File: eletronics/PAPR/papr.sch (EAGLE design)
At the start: 4 parts, among them Q1 FQP30N06L

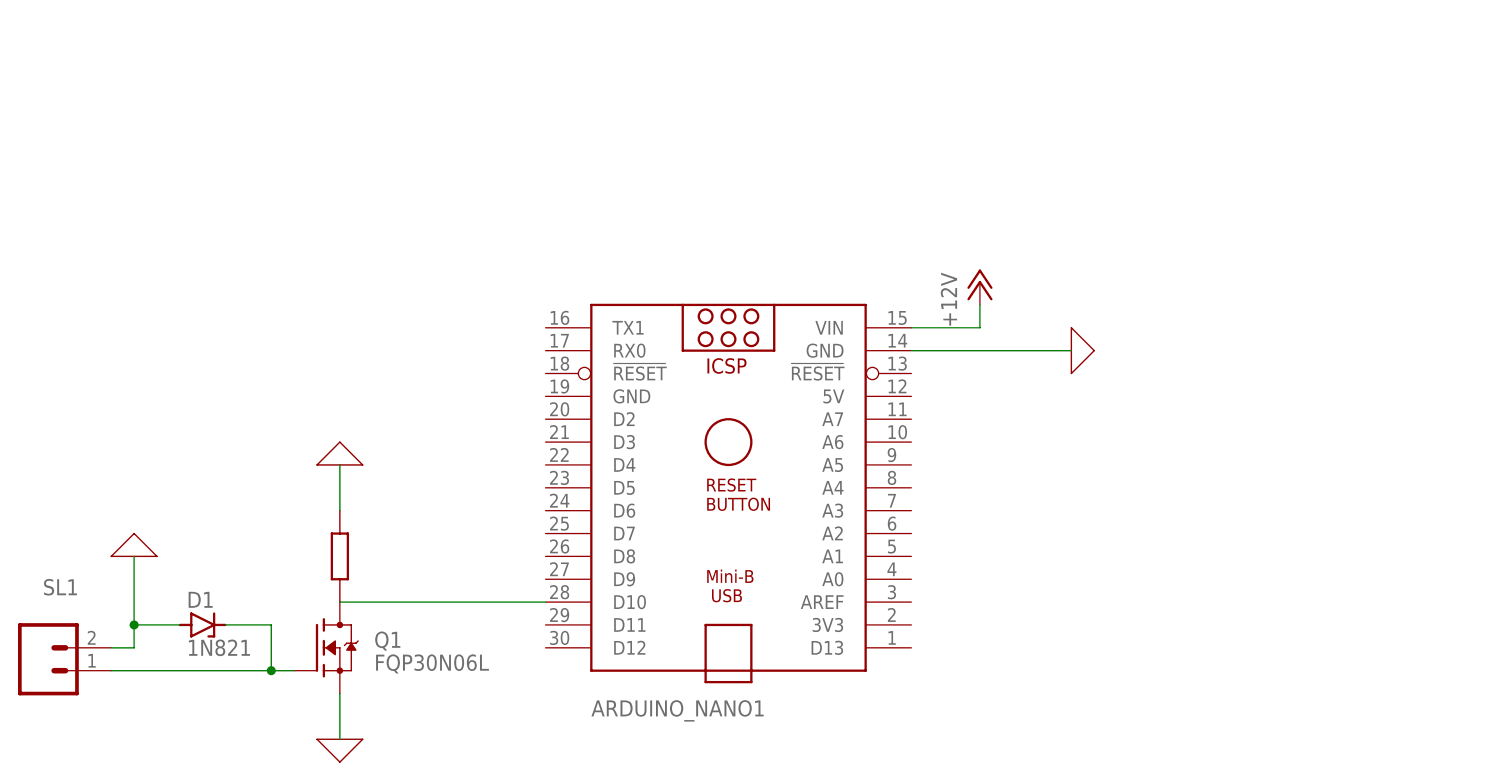
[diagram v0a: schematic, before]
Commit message: Made battery mount and working on basic electronics
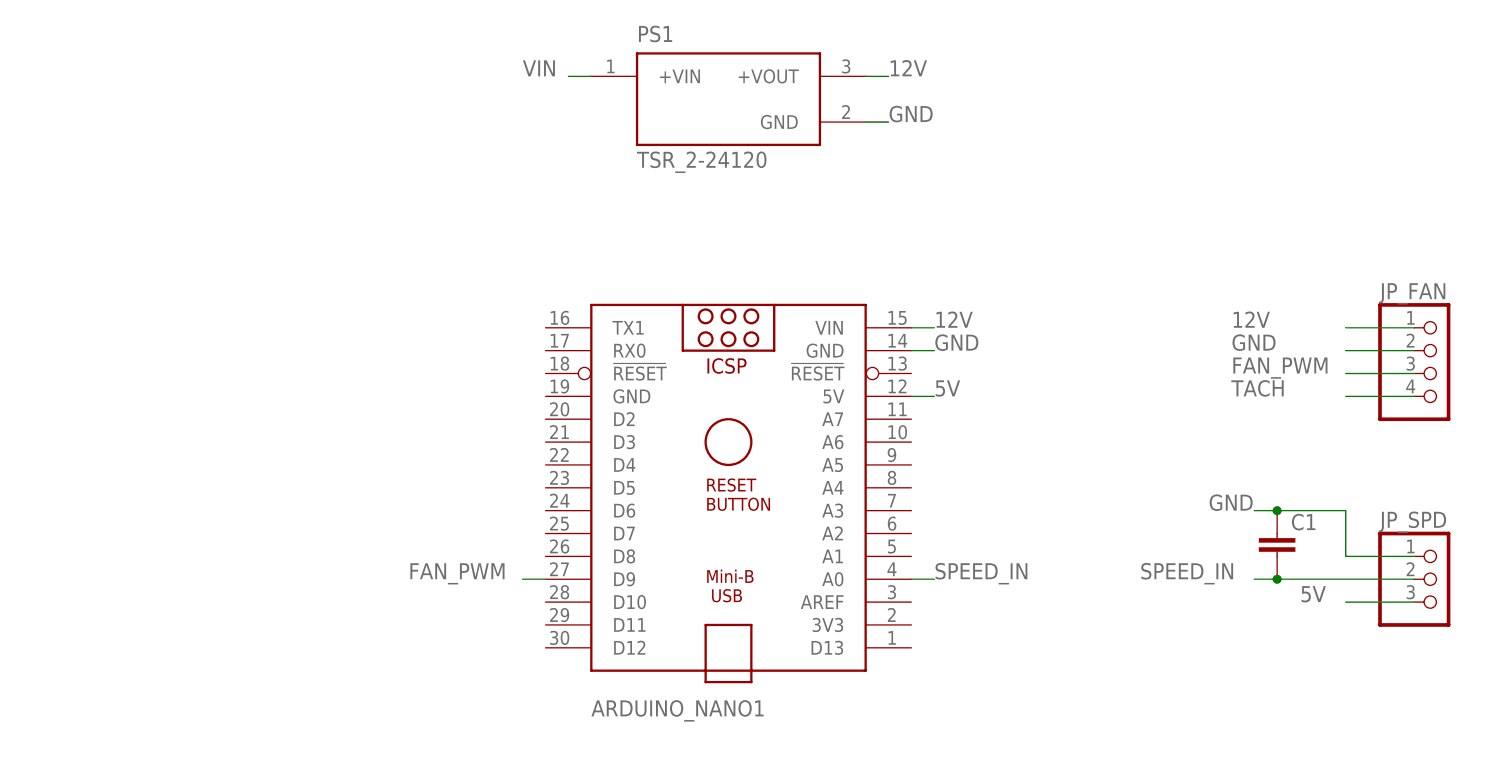
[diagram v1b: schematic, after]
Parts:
- removed D1: 1N821, diode:1N821
- removed Q1: FQP30N06L, FQP30N06L:FQP30N06L
- removed SL1: (no value), con-amp-quick:MA02
- added C1: (no value), capacitor-wima:C2,5-3
- added JP_FAN: (no value), pinhead:PINHD-1X4
- added JP_SPD: (no value), pinhead:PINHD-1X3
- added PS1: TSR_2-24120, TSR_2-24120:TSR_2-24120
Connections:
- removed net +12V: ARDUINO_NANO1.VIN
- removed net 0: ARDUINO_NANO1.GND@2, D1.A, Q1.S, SL1.2
- removed net N$1: ARDUINO_NANO1.D10, Q1.D
- removed net N$2: D1.C, Q1.G, SL1.1
- new net 12V: ARDUINO_NANO1.VIN, JP_FAN.1, PS1.+VOUT
- new net 5V: ARDUINO_NANO1.5V, JP_SPD.3
- new net FAN_PWM: ARDUINO_NANO1.D9, JP_FAN.3
- new net GND: ARDUINO_NANO1.GND@2, C1.1, JP_FAN.2, JP_SPD.1, PS1.GND
- new net SPEED_IN: ARDUINO_NANO1.A0, C1.2, JP_SPD.2
- new net TACH: JP_FAN.4
- new net VIN: PS1.+VIN
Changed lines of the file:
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@@
 <?xml version="1.0" encoding="utf-8"?>
 <!DOCTYPE eagle SYSTEM "eagle.dtd">
-<eagle version="9.5.2">
+<eagle version="9.6.1">
 <drawing>
 <settings>
@@
 <parts>
 <part name="ARDUINO_NANO1" library="ArduinoNanoV30" deviceset="ARDUINO_NANO" device=""/>
-<part name="Q1" library="FQP30N06L" deviceset="FQP30N06L" device=""/>
-<part name="D1" library="diode" library_urn="urn:adsk.eagle:library:210" deviceset="1N821" device="" package3d_urn="urn:adsk.eagle:package:43342/1"/>
-<part name="SL1" library="con-amp-quick" library_urn="urn:adsk.eagle:library:125" deviceset="MA02" device="" package3d_urn="urn:adsk.eagle:package:5970/1"/>
-<part name="P+1" library="supply1" library_urn="urn:adsk.eagle:library:371" deviceset="+12V" device=""/>
-<part name="X_1" library="ngspice-simulation" library_urn="urn:adsk.eagle:library:527439" deviceset="GND" device=""/>
-<part name="R1" library="docu-dummy" library_urn="urn:adsk.eagle:library:215" deviceset="R" device=""/>
-<part name="X_2" library="ngspice-simulation" library_urn="urn:adsk.eagle:library:527439" deviceset="GND" device=""/>
-<part name="X_4" library="ngspice-simulation" library_urn="urn:adsk.eagle:library:527439" deviceset="GND" device=""/>
-<part name="X_3" library="ngspice-simulation" library_urn="urn:adsk.eagle:library:527439" deviceset="GND" device=""/>
+<part name="PS1" library="TSR_2-24120" deviceset="TSR_2-24120" device=""/>
+<part name="JP_FAN" library="pinhead" library_urn="urn:adsk.eagle:library:325" deviceset="PINHD-1X4" device="" package3d_urn="urn:adsk.eagle:package:22407/2"/>
+<part name="JP_SPD" library="pinhead" library_urn="urn:adsk.eagle:library:325" deviceset="PINHD-1X3" device="" package3d_urn="urn:adsk.eagle:package:22458/2"/>
+<part name="C1" library="capacitor-wima" library_urn="urn:adsk.eagle:library:116" deviceset="C" device="2,5-3" package3d_urn="urn:adsk.eagle:package:5436/1"/>
 </parts>
 <sheets>
@@
 <attribute name="VALUE" x="35.56" y="30.48" size="1.778" layer="96"/>
 </instance>
-<instance part="Q1" gate="G$1" x="5.08" y="40.64" smashed="yes">
-<attribute name="VALUE" x="11.4264" y="38.1" size="1.778559375" layer="96"/>
-<attribute name="NAME" x="11.4196" y="40.64231875" size="1.77961875" layer="95"/>
-</instance>
-<instance part="D1" gate="1" x="-7.62" y="43.18" smashed="yes">
-<attribute name="NAME" x="-9.398" y="45.085" size="1.778" layer="95"/>
-<attribute name="VALUE" x="-9.398" y="39.751" size="1.778" layer="96"/>
-</instance>
-<instance part="SL1" gate="G$1" x="-25.4" y="38.1" smashed="yes">
-<attribute name="VALUE" x="-27.94" y="33.02" size="1.778" layer="96"/>
-<attribute name="NAME" x="-25.4" y="46.482" size="1.778" layer="95"/>
-</instance>
-<instance part="P+1" gate="1" x="78.74" y="81.28" smashed="yes">
-<attribute name="VALUE" x="76.2" y="76.2" size="1.778" layer="96" rot="R90"/>
-</instance>
-<instance part="X_1" gate="G$1" x="7.62" y="60.96" smashed="yes" rot="R180"/>
-<instance part="R1" gate="G$1" x="7.62" y="50.8" smashed="yes" rot="R90"/>
-<instance part="X_2" gate="G$1" x="7.62" y="30.48" smashed="yes"/>
-<instance part="X_4" gate="G$1" x="-15.24" y="50.8" smashed="yes" rot="R180"/>
-<instance part="X_3" gate="G$1" x="88.9" y="73.66" smashed="yes" rot="R90"/>
+<instance part="PS1" gate="G$1" x="50.8" y="101.6" smashed="yes">
+<attribute name="NAME" x="40.6361" y="107.9579" size="1.778" layer="95"/>
+<attribute name="VALUE" x="40.6386" y="93.9773" size="1.778" layer="96"/>
+</instance>
+<instance part="JP_FAN" gate="A" x="129.54" y="71.12" smashed="yes">
+<attribute name="NAME" x="123.19" y="79.375" size="1.778" layer="95"/>
+<attribute name="VALUE" x="123.19" y="63.5" size="1.778" layer="96"/>
+</instance>
+<instance part="JP_SPD" gate="A" x="129.54" y="48.26" smashed="yes">
+<attribute name="NAME" x="123.19" y="53.975" size="1.778" layer="95"/>
+<attribute name="VALUE" x="123.19" y="40.64" size="1.778" layer="96"/>
+</instance>
+<instance part="C1" gate="G$1" x="111.76" y="53.34" smashed="yes">
+<attribute name="NAME" x="113.284" y="53.721" size="1.778" layer="95"/>
+<attribute name="VALUE" x="113.284" y="48.641" size="1.778" layer="96"/>
+</instance>
 </instances>
 <busses>
 </busses>
 <nets>
-<net name="N$1" class="0">
-<segment>
-<pinref part="ARDUINO_NANO1" gate="G$1" pin="D10"/>
-<pinref part="Q1" gate="G$1" pin="D"/>
-<wire x1="30.48" y1="45.72" x2="7.62" y2="45.72" width="0.1524" layer="91"/>
-</segment>
-</net>
-<net name="0" class="0">
-<segment>
-<pinref part="X_1" gate="G$1" pin="0"/>
-<wire x1="7.62" y1="60.96" x2="7.62" y2="55.88" width="0.1524" layer="91"/>
-</segment>
-<segment>
-<pinref part="Q1" gate="G$1" pin="S"/>
-<pinref part="X_2" gate="G$1" pin="0"/>
-<wire x1="7.62" y1="35.56" x2="7.62" y2="30.48" width="0.1524" layer="91"/>
-</segment>
-<segment>
-<pinref part="SL1" gate="G$1" pin="2"/>
-<pinref part="X_4" gate="G$1" pin="0"/>
-<wire x1="-17.78" y1="40.64" x2="-15.24" y2="40.64" width="0.1524" layer="91"/>
-<wire x1="-15.24" y1="40.64" x2="-15.24" y2="43.18" width="0.1524" layer="91"/>
-<pinref part="D1" gate="1" pin="A"/>
-<wire x1="-15.24" y1="43.18" x2="-15.24" y2="50.8" width="0.1524" layer="91"/>
-<wire x1="-15.24" y1="43.18" x2="-10.16" y2="43.18" width="0.1524" layer="91"/>
-<junction x="-15.24" y="43.18"/>
+<net name="12V" class="0">
+<segment>
+<pinref part="ARDUINO_NANO1" gate="G$1" pin="VIN"/>
+<wire x1="71.12" y1="76.2" x2="73.66" y2="76.2" width="0.1524" layer="91"/>
+<label x="73.66" y="76.2" size="1.778" layer="95"/>
+</segment>
+<segment>
+<pinref part="PS1" gate="G$1" pin="+VOUT"/>
+<wire x1="66.04" y1="104.14" x2="68.58" y2="104.14" width="0.1524" layer="91"/>
+<label x="68.58" y="104.14" size="1.778" layer="95"/>
+</segment>
+<segment>
+<pinref part="JP_FAN" gate="A" pin="1"/>
+<wire x1="127" y1="76.2" x2="119.38" y2="76.2" width="0.1524" layer="91"/>
+<label x="106.68" y="76.2" size="1.778" layer="95"/>
+</segment>
+</net>
+<net name="GND" class="0">
+<segment>
+<pinref part="PS1" gate="G$1" pin="GND"/>
+<wire x1="66.04" y1="99.06" x2="68.58" y2="99.06" width="0.1524" layer="91"/>
+<label x="68.58" y="99.06" size="1.778" layer="95"/>
 </segment>
 <segment>
 <pinref part="ARDUINO_NANO1" gate="G$1" pin="GND@2"/>
-<pinref part="X_3" gate="G$1" pin="0"/>
-<wire x1="71.12" y1="73.66" x2="88.9" y2="73.66" width="0.1524" layer="91"/>
-</segment>
-</net>
-<net name="N$2" class="0">
-<segment>
-<pinref part="Q1" gate="G$1" pin="G"/>
-<pinref part="SL1" gate="G$1" pin="1"/>
-<wire x1="2.54" y1="38.1" x2="0" y2="38.1" width="0.1524" layer="91"/>
-<pinref part="D1" gate="1" pin="C"/>
-<wire x1="0" y1="38.1" x2="-17.78" y2="38.1" width="0.1524" layer="91"/>
-<wire x1="-5.08" y1="43.18" x2="0" y2="43.18" width="0.1524" layer="91"/>
-<wire x1="0" y1="43.18" x2="0" y2="38.1" width="0.1524" layer="91"/>
-<junction x="0" y="38.1"/>
-</segment>
-</net>
-<net name="+12V" class="0">
-<segment>
-<pinref part="ARDUINO_NANO1" gate="G$1" pin="VIN"/>
-<pinref part="P+1" gate="1" pin="+12V"/>
-<wire x1="71.12" y1="76.2" x2="78.74" y2="76.2" width="0.1524" layer="91"/>
-<wire x1="78.74" y1="76.2" x2="78.74" y2="78.74" width="0.1524" layer="91"/>
-</segment>
-</net>
+<wire x1="71.12" y1="73.66" x2="73.66" y2="73.66" width="0.1524" layer="91"/>
+<label x="73.66" y="73.66" size="1.778" layer="95"/>
+</segment>
+<segment>
+<pinref part="JP_FAN" gate="A" pin="2"/>
+<wire x1="127" y1="73.66" x2="119.38" y2="73.66" width="0.1524" layer="91"/>
+<label x="106.68" y="73.66" size="1.778" layer="95"/>
+</segment>
+<segment>
+<pinref part="JP_SPD" gate="A" pin="1"/>
+<wire x1="127" y1="50.8" x2="119.38" y2="50.8" width="0.1524" layer="91"/>
+<wire x1="119.38" y1="50.8" x2="119.38" y2="55.88" width="0.1524" layer="91"/>
+<wire x1="119.38" y1="55.88" x2="111.76" y2="55.88" width="0.1524" layer="91"/>
+<pinref part="C1" gate="G$1" pin="1"/>
+<wire x1="111.76" y1="55.88" x2="109.22" y2="55.88" width="0.1524" layer="91"/>
+<junction x="111.76" y="55.88"/>
+<label x="104.14" y="55.88" size="1.778" layer="95"/>
+</segment>
+</net>
+<net name="VIN" class="0">
+<segment>
+<pinref part="PS1" gate="G$1" pin="+VIN"/>
+<wire x1="35.56" y1="104.14" x2="33.02" y2="104.14" width="0.1524" layer="91"/>
+<label x="27.94" y="104.14" size="1.778" layer="95"/>
+</segment>
+</net>
+<net name="FAN_PWM" class="0">
+<segment>
+<pinref part="ARDUINO_NANO1" gate="G$1" pin="D9"/>
+<wire x1="30.48" y1="48.26" x2="27.94" y2="48.26" width="0.1524" layer="91"/>
+<label x="15.24" y="48.26" size="1.778" layer="95"/>
+</segment>
+<segment>
+<pinref part="JP_FAN" gate="A" pin="3"/>
+<wire x1="127" y1="71.12" x2="119.38" y2="71.12" width="0.1524" layer="91"/>
+<label x="106.68" y="71.12" size="1.778" layer="95"/>
+</segment>
+</net>
+<net name="SPEED_IN" class="0">
+<segment>
+<pinref part="ARDUINO_NANO1" gate="G$1" pin="A0"/>
+<wire x1="71.12" y1="48.26" x2="73.66" y2="48.26" width="0.1524" layer="91"/>
+<label x="73.66" y="48.26" size="1.778" layer="95"/>
+</segment>
+<segment>
+<pinref part="JP_SPD" gate="A" pin="2"/>
+<wire x1="127" y1="48.26" x2="111.76" y2="48.26" width="0.1524" layer="91"/>
+<pinref part="C1" gate="G$1" pin="2"/>
+<wire x1="111.76" y1="48.26" x2="109.22" y2="48.26" width="0.1524" layer="91"/>
+<junction x="111.76" y="48.26"/>
+<label x="96.52" y="48.26" size="1.778" layer="95"/>
+</segment>
+</net>
+<net name="TACH" class="0">
+<segment>
+<pinref part="JP_FAN" gate="A" pin="4"/>
+<wire x1="127" y1="68.58" x2="119.38" y2="68.58" width="0.1524" layer="91"/>
+<label x="106.68" y="68.58" size="1.778" layer="95"/>
+</segment>
+</net>
+<net name="5V" class="0">
+<segment>
+<pinref part="JP_SPD" gate="A" pin="3"/>
+<wire x1="127" y1="45.72" x2="119.38" y2="45.72" width="0.1524" layer="91"/>
+<label x="114.3" y="45.72" size="1.778" layer="95"/>
+</segment>
+<segment>
+<pinref part="ARDUINO_NANO1" gate="G$1" pin="5V"/>
+<wire x1="71.12" y1="68.58" x2="73.66" y2="68.58" width="0.1524" layer="91"/>
+<label x="73.66" y="68.58" size="1.778" layer="95"/>
+</segment>
+</net>

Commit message: Checkpoint
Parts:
- added JP1: (no value), pinhead:PINHD-1X2
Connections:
- net GND: now also JP1.2
- net VIN: now also JP1.1
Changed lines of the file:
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@@
 <part name="JP_SPD" library="pinhead" library_urn="urn:adsk.eagle:library:325" deviceset="PINHD-1X3" device="" package3d_urn="urn:adsk.eagle:package:22458/2"/>
 <part name="C1" library="capacitor-wima" library_urn="urn:adsk.eagle:library:116" deviceset="C" device="2,5-3" package3d_urn="urn:adsk.eagle:package:5436/1"/>
+<part name="JP1" library="pinhead" library_urn="urn:adsk.eagle:library:325" deviceset="PINHD-1X2" device="" package3d_urn="urn:adsk.eagle:package:22435/2"/>
 </parts>
 <sheets>
@@
 <attribute name="NAME" x="113.284" y="53.721" size="1.778" layer="95"/>
 <attribute name="VALUE" x="113.284" y="48.641" size="1.778" layer="96"/>
+</instance>
+<instance part="JP1" gate="G$1" x="129.54" y="99.06" smashed="yes">
+<attribute name="NAME" x="123.19" y="104.775" size="1.778" layer="95"/>
+<attribute name="VALUE" x="123.19" y="93.98" size="1.778" layer="96"/>
 </instance>
 </instances>
@@
 <label x="104.14" y="55.88" size="1.778" layer="95"/>
 </segment>
+<segment>
+<pinref part="JP1" gate="G$1" pin="2"/>
+<wire x1="127" y1="99.06" x2="119.38" y2="99.06" width="0.1524" layer="91"/>
+<label x="114.3" y="99.06" size="1.778" layer="95"/>
+</segment>
 </net>
 <net name="VIN" class="0">
@@
 <label x="27.94" y="104.14" size="1.778" layer="95"/>
 </segment>
+<segment>
+<pinref part="JP1" gate="G$1" pin="1"/>
+<wire x1="127" y1="101.6" x2="119.38" y2="101.6" width="0.1524" layer="91"/>
+<label x="114.3" y="101.6" size="1.778" layer="95"/>
+</segment>
 </net>
